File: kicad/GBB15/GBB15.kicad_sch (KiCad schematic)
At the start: 74 parts, among them J1 CAN_IN, J10 USB-C, J2 CAN_OUT, J3 MA_THERM, J4 MB_THERM, J5 MA, J6 MB, J7 ENDSTOP1, J8 ENDSTOP2, SW1 BOOT, SW2 RESET, U1 TMC2209-LA-T, U2 STM32G0B1CEU6, U3 TMC2209-LA-T, U4 MAX3051EKA+T, U5 NCP730BMT330TBG, Y1 Crystal_GND24

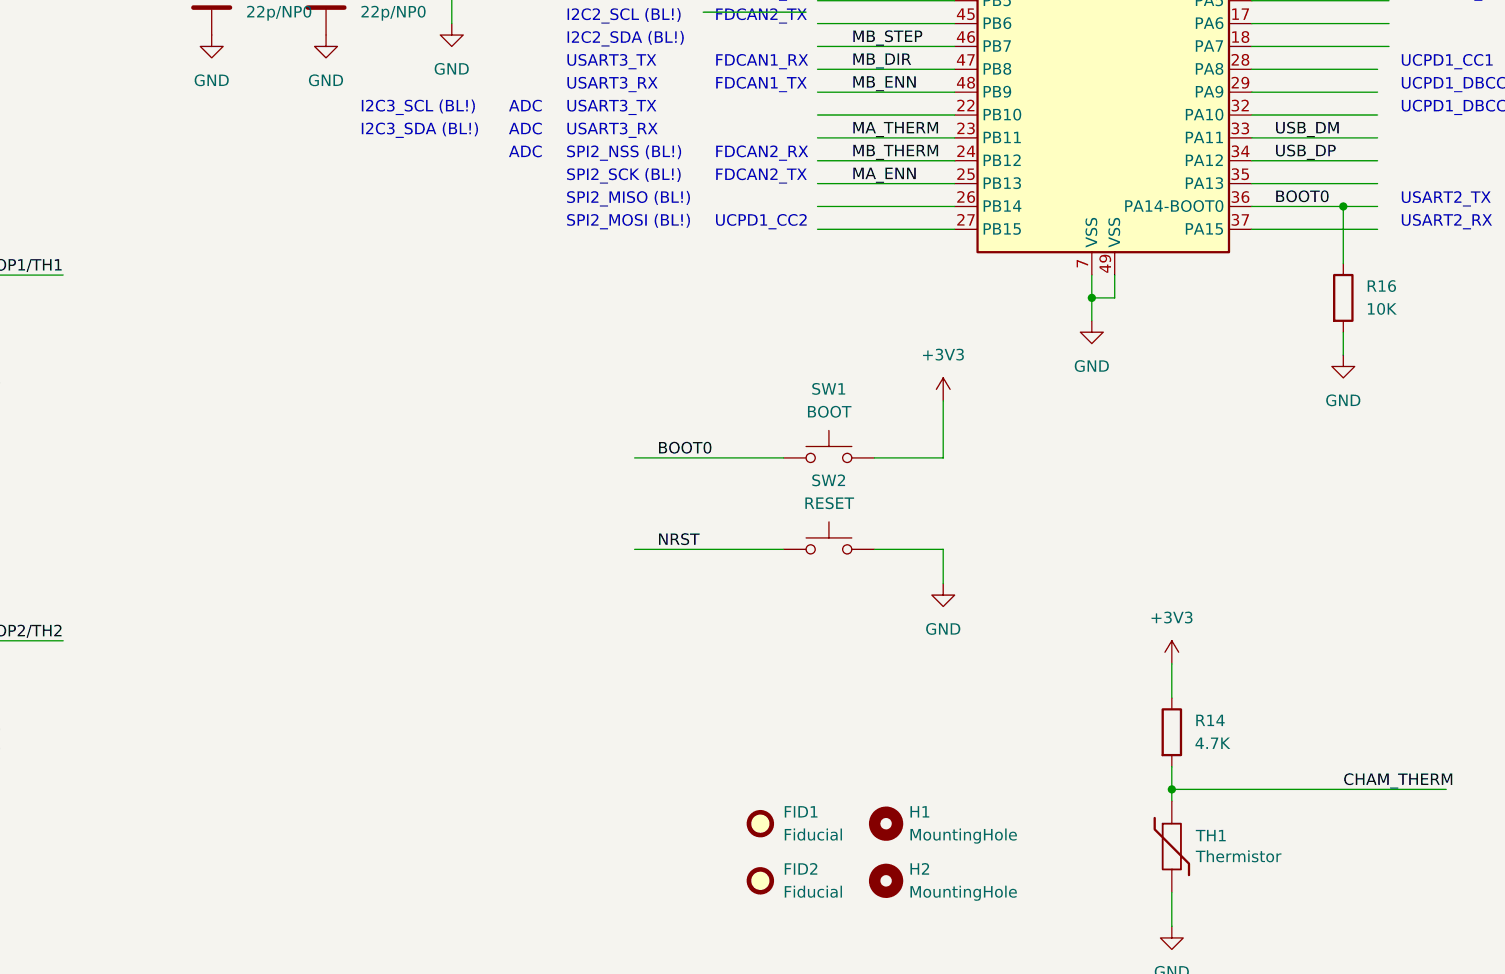
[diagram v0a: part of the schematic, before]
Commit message: Added additional debug pads for SWD
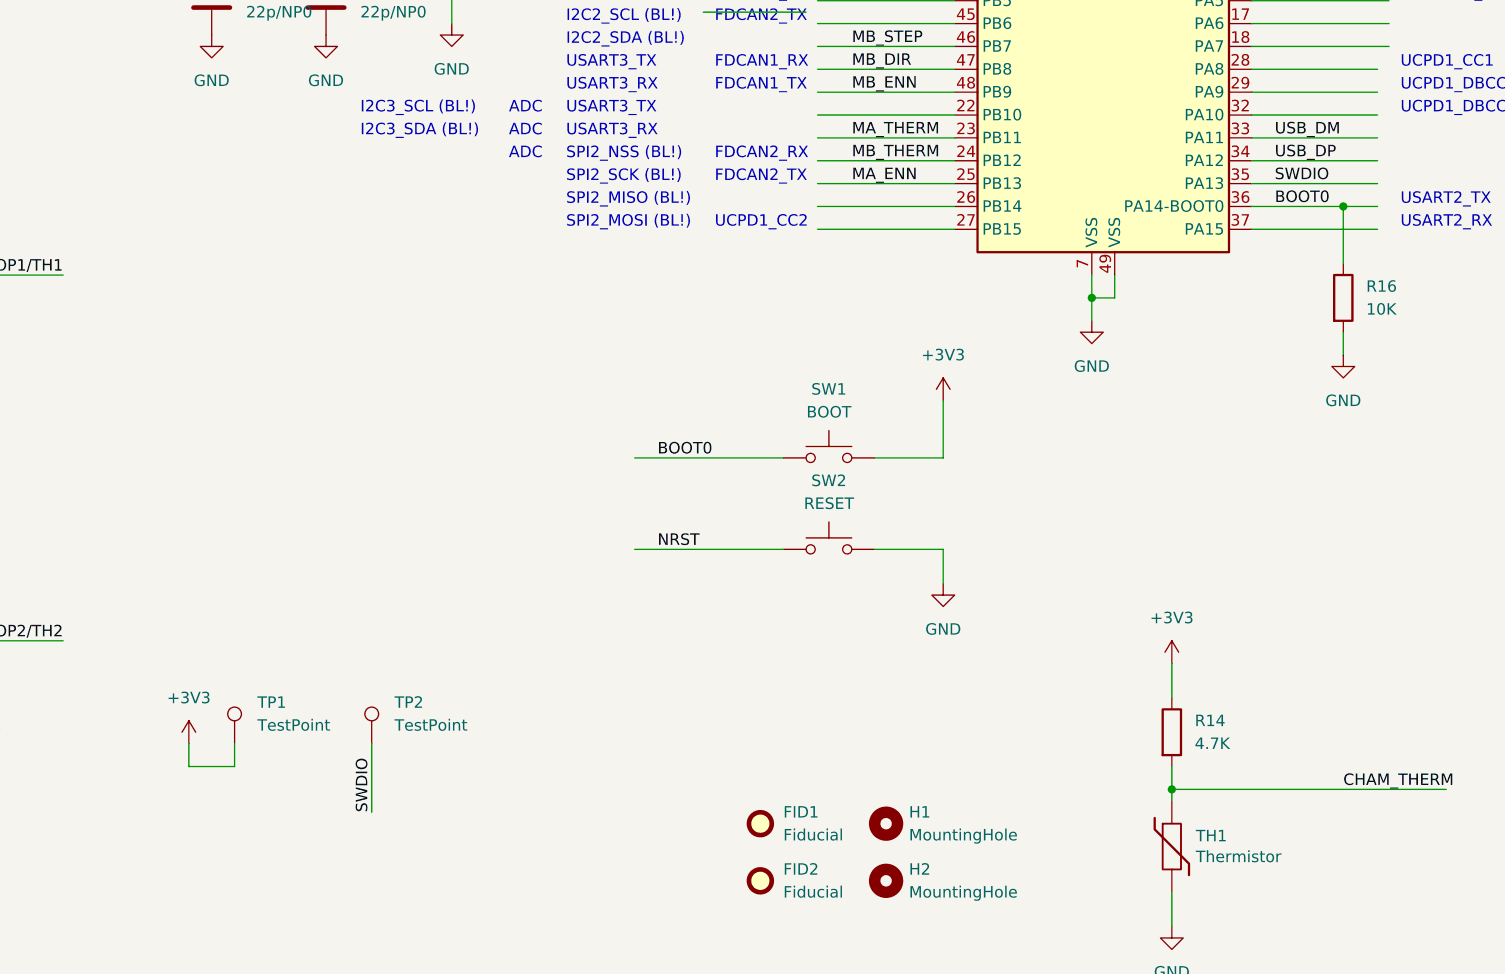
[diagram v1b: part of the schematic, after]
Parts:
- added TP1, TP2: TestPoint, TestPoint:TestPoint_Pad_1.5x1.5mm, symbol Connector:TestPoint
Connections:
- net +3V3: now also TP1.1
- net SWDIO: now reaches U2.35 (PA13)
- net SWDIO: now also TP2.1
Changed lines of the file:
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@@
     (stroke (width 0) (type default) (color 0 0 0 0))
   )
+  (wire (pts (xy 93.98 243.84) (xy 99.06 243.84))
+    (stroke (width 0) (type default) (color 0 0 0 0))
+  )
   (wire (pts (xy 328.93 88.9) (xy 330.2 88.9))
     (stroke (width 0) (type default) (color 0 0 0 0))
@@
     (stroke (width 0) (type default) (color 0 0 0 0))
   )
+  (wire (pts (xy 99.06 243.84) (xy 99.06 241.3))
+    (stroke (width 0) (type default) (color 0 0 0 0))
+  )
   (wire (pts (xy 367.03 46.99) (xy 372.11 46.99))
     (stroke (width 0) (type default) (color 0 0 0 0))
@@
     (stroke (width 0) (type default) (color 0 0 0 0))
   )
+  (wire (pts (xy 93.98 241.3) (xy 93.98 243.84))
+    (stroke (width 0) (type default) (color 0 0 0 0))
+  )
   (wire (pts (xy 187.96 45.72) (xy 207.01 45.72))
     (stroke (width 0) (type default) (color 0 0 0 0))
@@
     (stroke (width 0) (type default) (color 0 0 0 0))
   )
+  (wire (pts (xy 114.3 241.3) (xy 114.3 248.92))
+    (stroke (width 0) (type default) (color 0 0 0 0))
+  )
   (wire (pts (xy 364.49 21.59) (xy 364.49 24.13))
     (stroke (width 0) (type default) (color 0 0 0 0))
@@
     (effects (font (size 1.27 1.27)) (justify left bottom))
   )
+  (label "SWDIO" (at 114.3 248.92 90)
+    (effects (font (size 1.27 1.27)) (justify left bottom))
+  )
   (label "MB_B2" (at 349.25 187.96 0)
     (effects (font (size 1.27 1.27)) (justify left bottom))
@@
     (effects (font (size 1.27 1.27)) (justify left bottom))
   )
+  (label "SWDIO" (at 214.63 179.07 0)
+    (effects (font (size 1.27 1.27)) (justify left bottom))
+  )
   (label "MB_DIAG" (at 167.64 158.75 0)
     (effects (font (size 1.27 1.27)) (justify left bottom))
@@
     (pin "1")
   )
+  (symbol (lib_id "Connector:TestPoint") (at 114.3 241.3 0) (unit 1)
+    (in_bom yes) (on_board yes) (fields_autoplaced)
+    (property "Reference" "TP2" (id 0) (at 116.84 236.7279 0)
+      (effects (font (size 1.27 1.27)) (justify left))
+    )
+    (property "Value" "TestPoint" (id 1) (at 116.84 239.2679 0)
+      (effects (font (size 1.27 1.27)) (justify left))
+    )
+    (property "Footprint" "TestPoint:TestPoint_Pad_1.5x1.5mm" (id 2) (at 119.38 241.3 0)
+      (effects (font (size 1.27 1.27)) hide)
+    )
+    (property "Datasheet" "~" (id 3) (at 119.38 241.3 0)
+      (effects (font (size 1.27 1.27)) hide)
+    )
+    (pin "1")
+  )
   (symbol (lib_id "power:+3V3") (at 369.57 106.68 0) (unit 1)
     (in_bom yes) (on_board yes) (fields_autoplaced)
@@
     (pin "1")
   )
+  (symbol (lib_id "power:+3V3") (at 93.98 241.3 0) (unit 1)
+    (in_bom yes) (on_board yes) (fields_autoplaced)
+    (property "Reference" "#PWR0178" (id 0) (at 93.98 245.11 0)
+      (effects (font (size 1.27 1.27)) hide)
+    )
+    (property "Value" "+3V3" (id 1) (at 93.98 236.22 0))
+    (property "Footprint" "" (id 2) (at 93.98 241.3 0)
+      (effects (font (size 1.27 1.27)) hide)
+    )
+    (property "Datasheet" "" (id 3) (at 93.98 241.3 0)
+      (effects (font (size 1.27 1.27)) hide)
+    )
+    (pin "1")
+  )
   (symbol (lib_id "Device:C_Polarized") (at 364.49 160.02 0) (unit 1)
     (in_bom yes) (on_board yes) (fields_autoplaced)
@@
     (pin "2")
   )
+  (symbol (lib_id "Connector:TestPoint") (at 99.06 241.3 0) (unit 1)
+    (in_bom yes) (on_board yes) (fields_autoplaced)
+    (property "Reference" "TP1" (id 0) (at 101.6 236.7279 0)
+      (effects (font (size 1.27 1.27)) (justify left))
+    )
+    (property "Value" "TestPoint" (id 1) (at 101.6 239.2679 0)
+      (effects (font (size 1.27 1.27)) (justify left))
+    )
+    (property "Footprint" "TestPoint:TestPoint_Pad_1.5x1.5mm" (id 2) (at 104.14 241.3 0)
+      (effects (font (size 1.27 1.27)) hide)
+    )
+    (property "Datasheet" "~" (id 3) (at 104.14 241.3 0)
+      (effects (font (size 1.27 1.27)) hide)
+    )
+    (pin "1")
+  )
   (symbol (lib_id "Device:FerriteBead") (at 135.89 45.72 90) (unit 1)
     (in_bom yes) (on_board yes) (fields_autoplaced)
@@
       (reference "#PWR0177") (unit 1) (value "GND") (footprint "")
     )
+    (path "/4740cc75-4717-4c4f-8c0d-4cb2a642c90a"
+      (reference "#PWR0178") (unit 1) (value "+3V3") (footprint "")
+    )
     (path "/26182999-0393-4015-be74-1214d882a51e"
       (reference "C1") (unit 1) (value "100u/35V/105°C") (footprint "Capacitor_THT:CP_Radial_D6.3mm_P2.50mm")
@@
       (reference "TH1") (unit 1) (value "Thermistor") (footprint "Resistor_SMD:R_0603_1608Metric")
     )
+    (path "/b7fbc045-bf47-46c2-9daa-ff845429b376"
+      (reference "TP1") (unit 1) (value "TestPoint") (footprint "TestPoint:TestPoint_Pad_1.5x1.5mm")
+    )
+    (path "/40bd5766-cdff-47b4-b15b-0032560dd450"
+      (reference "TP2") (unit 1) (value "TestPoint") (footprint "TestPoint:TestPoint_Pad_1.5x1.5mm")
+    )
     (path "/2f18ffad-7e01-4f2f-b098-f60c5076a1c5"
